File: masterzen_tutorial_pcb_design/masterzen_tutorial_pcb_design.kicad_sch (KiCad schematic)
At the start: 15 parts, among them J1 AVR-ISP-6, U1 ATmega32U4-A, Y1 Crystal_GND24_Small

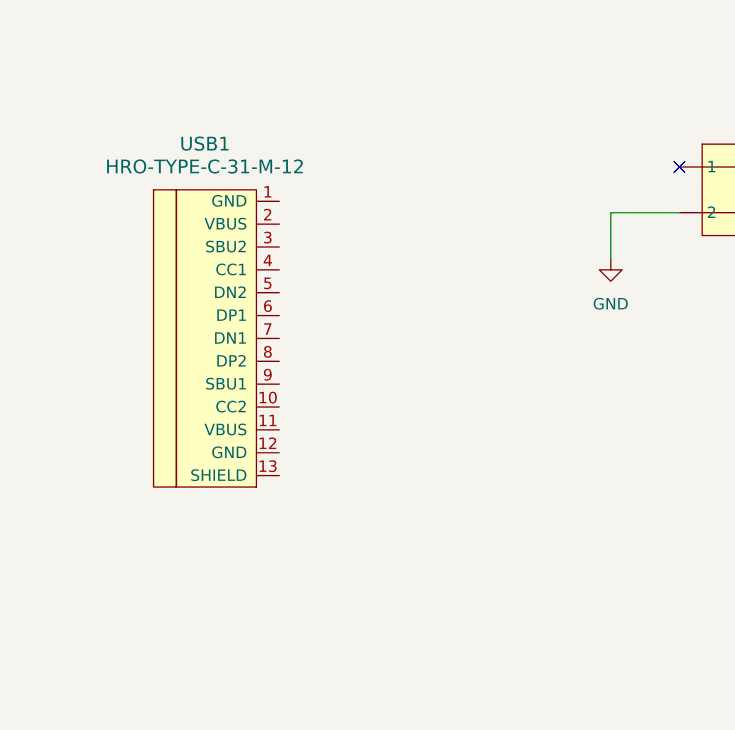
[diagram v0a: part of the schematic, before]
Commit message: added connected some of the USB lines
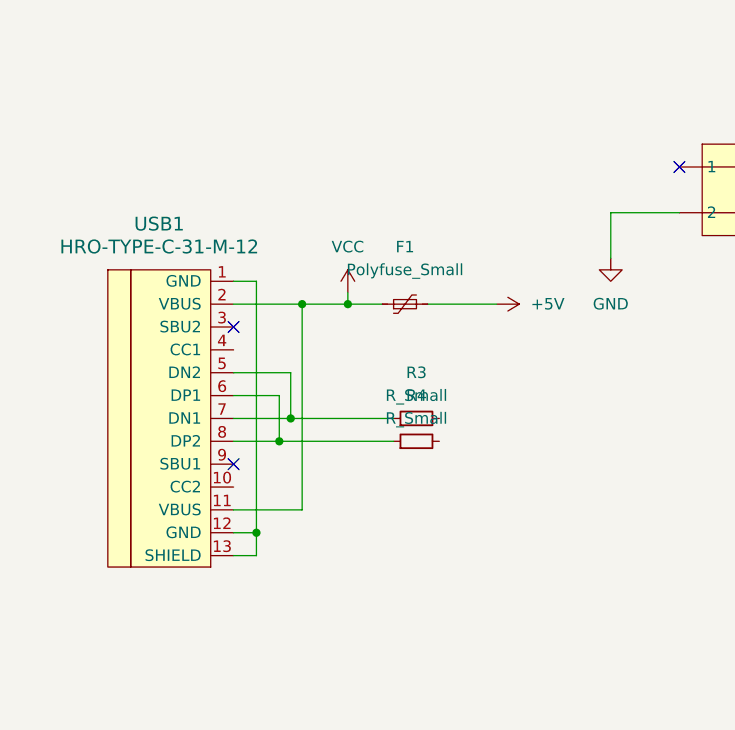
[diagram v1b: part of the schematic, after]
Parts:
- added F1: Polyfuse_Small, symbol Device:Polyfuse_Small
- added R3, R4: R_Small, symbol Device:R_Small
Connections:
- net +5V: now also F1.2
- net at USB1.1 (GND): now also USB1.12 (GND), USB1.13 (SHIELD)
- net VCC: now reaches USB1.11 (VBUS)
- net VCC: now also USB1.2 (VBUS), F1.1
- net at USB1.5 (DN2): now also USB1.7 (DN1), R3.1
- net at USB1.6 (DP1): now also USB1.8 (DP2), R4.1
- no-connect marks 3 -> 5
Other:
- moved on the sheet: USB1

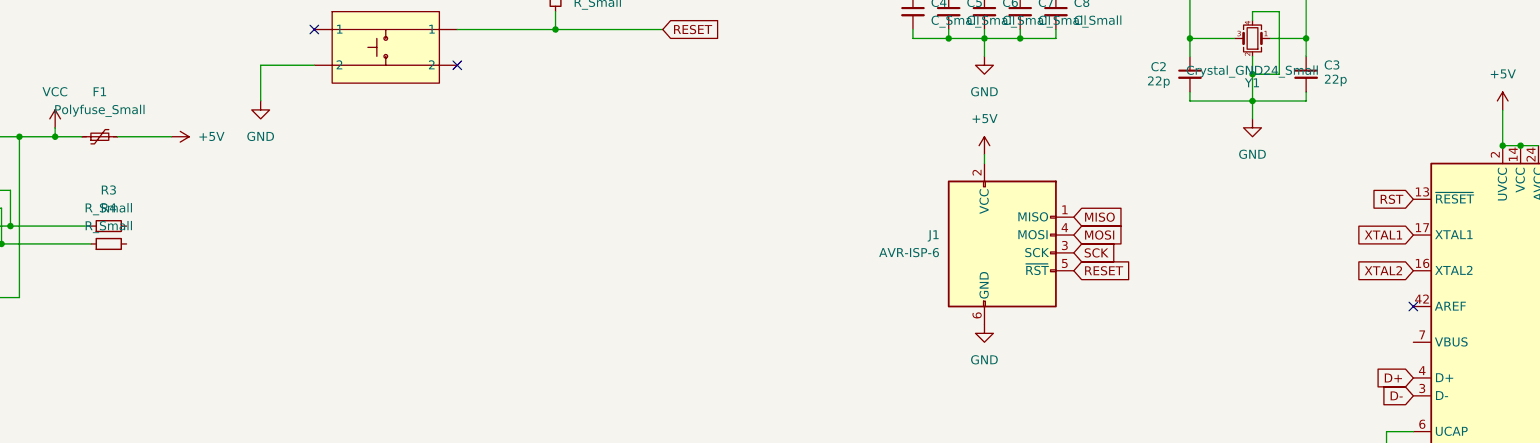
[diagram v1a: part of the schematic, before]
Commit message: added d+ and d- to usb header
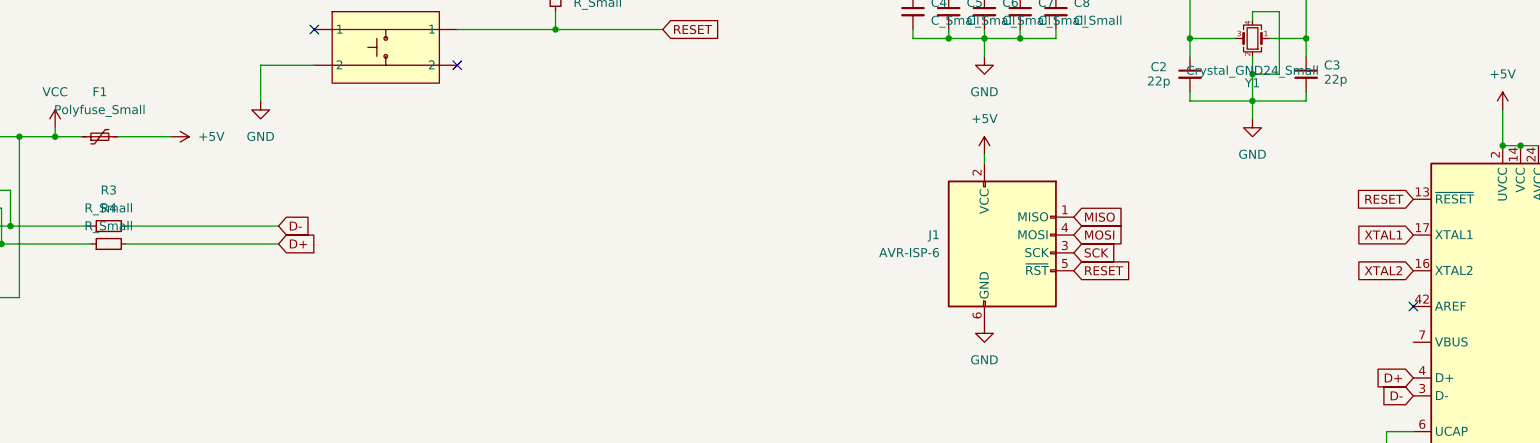
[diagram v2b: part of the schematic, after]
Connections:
- net RST is gone; now on net RESET: U1.13 (~{RESET})
- net D+: now also R4.2
- net D-: now also R3.2
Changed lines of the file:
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@@
+	(wire
+		(pts
+			(xy 55.88 58.42) (xy 77.47 58.42)
+		)
+		(stroke
+			(width 0)
+			(type default)
+		)
+	)
 	(wire
 		(pts
@@
 		(pts
 			(xy 251.46 138.43) (xy 254 138.43)
+		)
+		(stroke
+			(width 0)
+			(type default)
+		)
+	)
+	(wire
+		(pts
+			(xy 55.88 60.96) (xy 77.47 60.96)
 		)
 		(stroke
@@
 	(global_label "D+"
 		(shape input)
-		(at 238.76 80.01 180)
+		(at 77.47 60.96 0)
 		(fields_autoplaced yes)
 		(effects
@@
 				(size 1.27 1.27)
 			)
+			(justify left)
+		)
+		(property "Intersheetrefs" "${INTERSHEET_REFS}"
+			(at 83.2976 60.96 0)
+			(effects
+				(font
+					(size 1.27 1.27)
+				)
+				(justify left)
+				(hide yes)
+			)
+		)
+	)
+	(global_label "D+"
+		(shape input)
+		(at 238.76 80.01 180)
+		(fields_autoplaced yes)
+		(effects
+			(font
+				(size 1.27 1.27)
+			)
 			(justify right)
 		)
@@
 		)
 	)
+	(global_label "D-"
+		(shape input)
+		(at 77.47 58.42 0)
+		(fields_autoplaced yes)
+		(effects
+			(font
+				(size 1.27 1.27)
+			)
+			(justify left)
+		)
+		(property "Intersheetrefs" "${INTERSHEET_REFS}"
+			(at 83.2976 58.42 0)
+			(effects
+				(font
+					(size 1.27 1.27)
+				)
+				(justify left)
+				(hide yes)
+			)
+		)
+	)
 	(global_label "RESET"
 		(shape input)
@@
 		)
 	)
-	(global_label "RST"
+	(global_label "RESET"
 		(shape input)
 		(at 238.76 54.61 180)
@@
 		)
 		(property "Intersheetrefs" "${INTERSHEET_REFS}"
-			(at 232.3277 54.61 0)
+			(at 230.0297 54.61 0)
 			(effects
 				(font
@@
 		)
 		(instances
-			(project ""
+			(project "masterzen_tutorial_pcb_design"
 				(path "/43ab7f41-8dc3-471f-b30f-d5100c2539fd"
 					(reference "#PWR013")
@@
 		)
 		(instances
-			(project ""
+			(project "masterzen_tutorial_pcb_design"
 				(path "/43ab7f41-8dc3-471f-b30f-d5100c2539fd"
 					(reference "R4")
@@
 		)
 		(instances
-			(project ""
+			(project "masterzen_tutorial_pcb_design"
 				(path "/43ab7f41-8dc3-471f-b30f-d5100c2539fd"
 					(reference "#PWR012")
@@
 		)
 		(instances
-			(project ""
+			(project "masterzen_tutorial_pcb_design"
 				(path "/43ab7f41-8dc3-471f-b30f-d5100c2539fd"
 					(reference "R3")
@@
 		)
 		(instances
-			(project ""
+			(project "masterzen_tutorial_pcb_design"
 				(path "/43ab7f41-8dc3-471f-b30f-d5100c2539fd"
 					(reference "F1")

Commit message: finished part 1
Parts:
- added R5, R6: R_Small, symbol Device:R_Small
- added U3: PRTR5V0U2X, symbol random-keyboard-parts:PRTR5V0U2X
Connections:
- net D+: now also U3.3 (IO2)
- net D-: now also U3.2 (IO1)
- net GND: now also USB1.1 (GND), USB1.12 (GND), USB1.13 (SHIELD), R5.2, R6.2, U3.1 (GND)
- net VCC: now also U3.4 (VCC)
- net at USB1.10 (CC2): now also R5.1
- net at USB1.4 (CC1): now also R6.1
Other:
- moved on the sheet: R2, U2

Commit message: initial matrix
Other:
- added sheet matrix (untitled.kicad_sch)
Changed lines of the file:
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@@
+		)
+	)
+	(sheet
+		(at 96.52 104.14)
+		(size 12.7 3.81)
+		(fields_autoplaced yes)
+		(stroke
+			(width 0.1524)
+			(type solid)
+		)
+		(fill
+			(color 0 0 0 0.0000)
+		)
+		(property "Sheetname" "matrix"
+			(at 96.52 103.4284 0)
+			(effects
+				(font
+					(size 1.27 1.27)
+				)
+				(justify left bottom)
+			)
+		)
+		(property "Sheetfile" "untitled.kicad_sch"
+			(at 96.52 108.5346 0)
+			(effects
+				(font
+					(size 1.27 1.27)
+				)
+				(justify left top)
+			)
+		)
+		(instances
+			(project "masterzen_tutorial_pcb_design"
+				(path "/43ab7f41-8dc3-471f-b30f-d5100c2539fd"
+					(page "2")
+				)
+			)
 		)
 	)

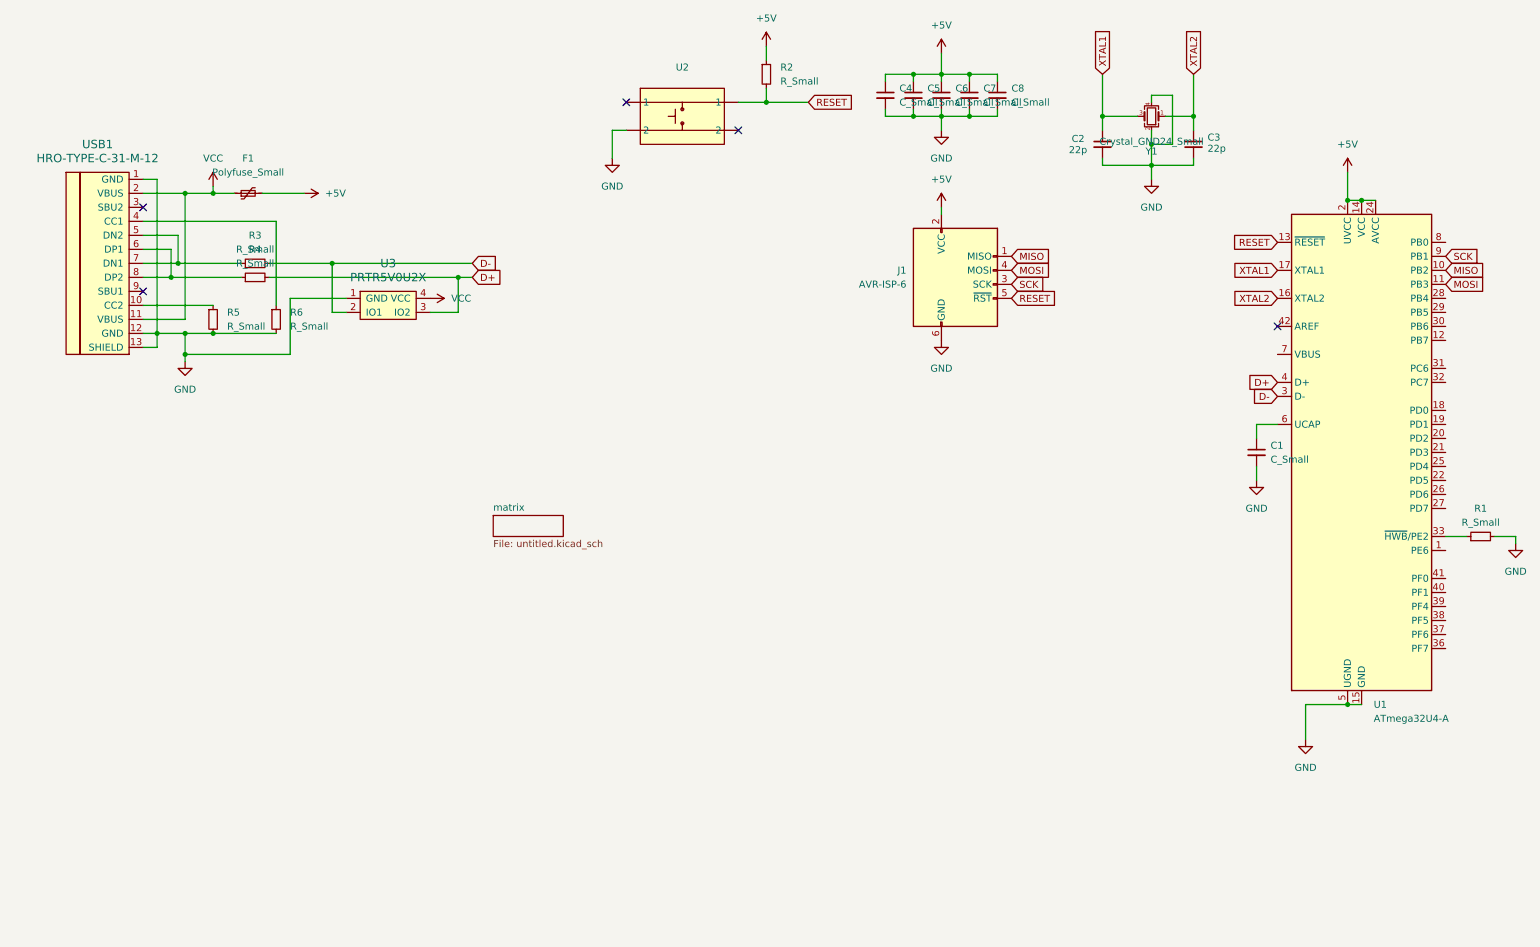
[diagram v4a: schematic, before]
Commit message: switched micro to the STM32F303
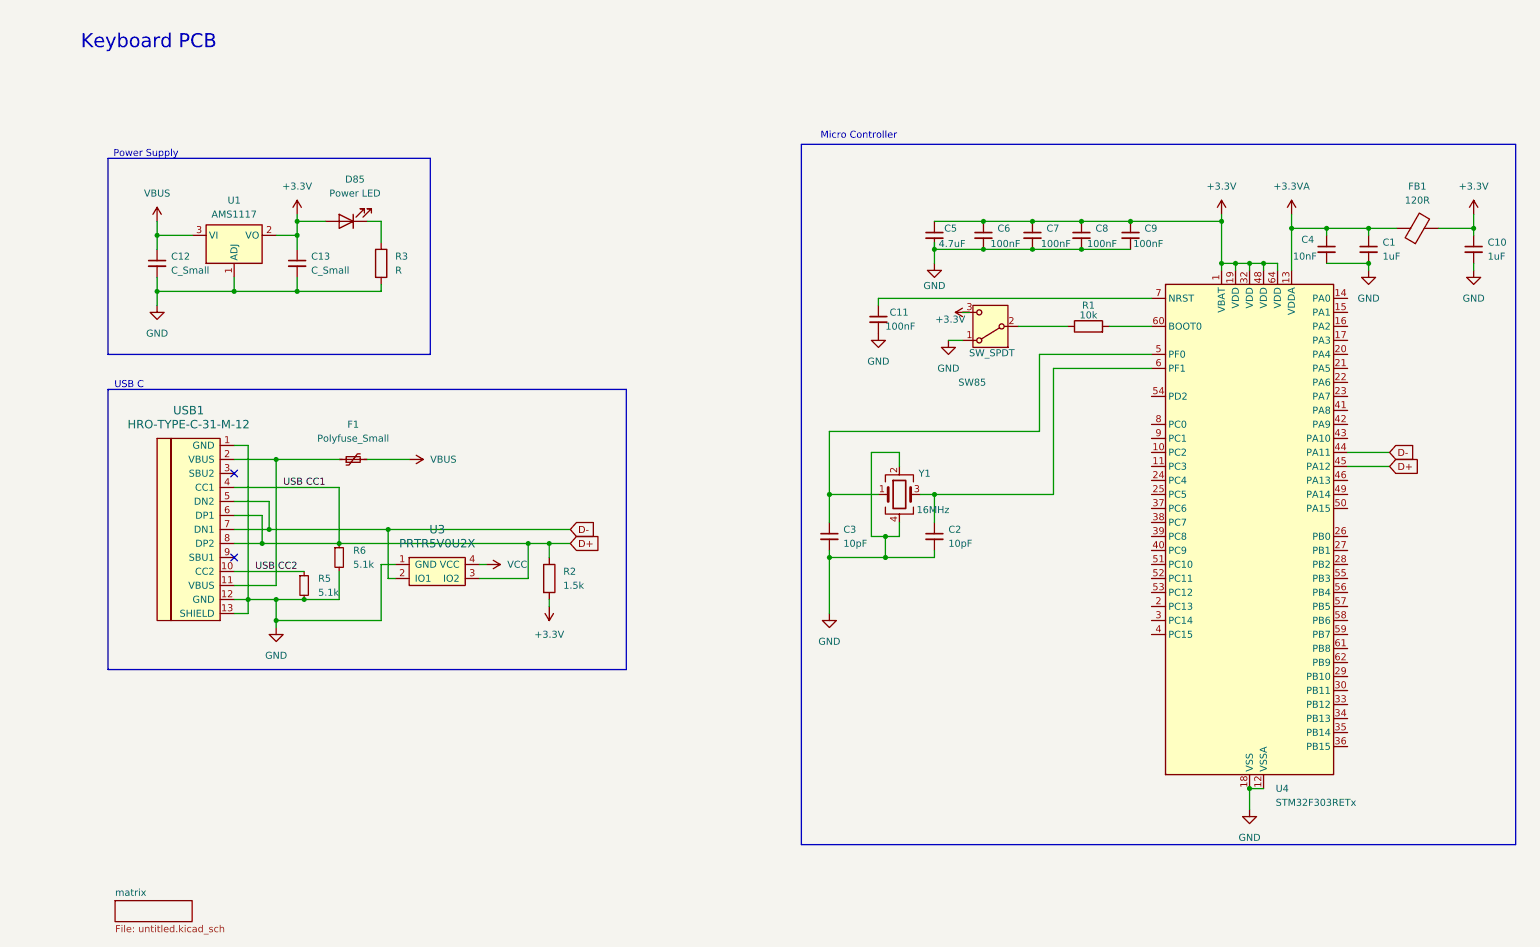
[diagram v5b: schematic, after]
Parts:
- removed J1: AVR-ISP-6, symbol Connector:AVR-ISP-6
- removed R1, R2, R3, R4: R_Small, symbol Device:R_Small
- removed U1: ATmega32U4-A, Package_QFP:TQFP-44_10x10mm_P0.8mm, symbol MCU_Microchip_ATmega:ATmega32U4-A
- removed U2: ~, symbol SW_PUSH:SW_SKQG
- removed Y1: Crystal_GND24_Small, symbol Device:Crystal_GND24_Small
- added C10: 1uF, symbol Device:C_Small
- added C11, C9: 100nF, symbol Device:C_Small
- added C12, C13: C_Small, symbol Device:C_Small
- added D85: Power LED, symbol Device:LED
- added FB1: 120R, symbol Device:FerriteBead
- added R1: 10k, symbol Device:R
- added R2: 1.5k, symbol Device:R
- added R3: R, symbol Device:R
- added SW85: SW_SPDT, symbol Switch:SW_SPDT
- added U1: AMS1117, Package_TO_SOT_SMD:SOT-223-3_TabPin2, symbol Regulator_Linear:AMS1117
- added U4: STM32F303RETx, Package_QFP:LQFP-64_10x10mm_P0.5mm, symbol MCU_ST_STM32F3:STM32F303RETx
- added Y1: 16MHz, symbol Device:Crystal_GND24
- C1: value C_Small -> 1uF
- C2, C3: value 22p -> 10pF
- C4: value C_Small -> 10nF
- C5: value C_Small -> 4.7uF
- C6, C7, C8: value C_Small -> 100nF
- R5, R6: value R_Small -> 5.1k
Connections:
- net D+: now also R6.1, USB1.4 (CC1), USB1.6 (DP1), USB1.8 (DP2), R2.1, U4.45 (PA12)
- net D-: now also USB1.5 (DN2), USB1.7 (DN1), U4.44 (PA11)
- net GND: now also C10.2, C11.2, C12.2, C13.2, C9.2, R3.2, SW85.1 (A), U1.1 (ADJ), U4.12 (VSSA), U4.18 (VSS), U4.31 (VSS), U4.47 (VSS), U4.63 (VSS), Y1.2, Y1.4
- net VCC: no longer F1.1, USB1.11 (VBUS), USB1.2 (VBUS)
- net +3.3VA: now reaches C1.1
- net +3.3VA: now also C4.1, FB1.1, U4.13 (VDDA)
- net USB CC2: now reaches R5.1, USB1.10 (CC2)
- net +5V renamed +3.3V
- net +3.3V: now also C10.1, C13.1, C9.1, D85.2 (A), FB1.2, R2.2, SW85.3 (C), U1.2 (VO), U4.1 (VBAT), U4.19 (VDD), U4.32 (VDD), U4.48 (VDD), U4.64 (VDD); no longer C4.1, F1.2
- net XTAL1: no longer names the net of C2.1
- net XTAL1: now also U4.6 (PF1), Y1.3
- net XTAL2: no longer names the net of C3.1
- net XTAL2: now also U4.5 (PF0), Y1.1
- new net: D85.1 (K), R3.1
- new net: R1.1, SW85.2 (B)
- new net: R1.2, U4.60 (BOOT0)
- new net: C11.1, U4.7 (NRST)
- new net: F1.1, USB1.11 (VBUS), USB1.2 (VBUS)
- new net VBUS: C12.1, F1.2, U1.3 (VI)
- no-connect marks 5 -> 2
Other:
- note added: "Keyboard PCB"
- note added: "Micro Controller"
- note added: "Power Supply"
- note added: "USB C"
- moved on the sheet: F1, R5, R6, U3, USB1
